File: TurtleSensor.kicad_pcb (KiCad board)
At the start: 2 copper layers, 30 x 30 mm, 14 parts, among them IC1 ATMEGA328P-A, J2 FTDIConnector, U1 SI7021, U2 M24512

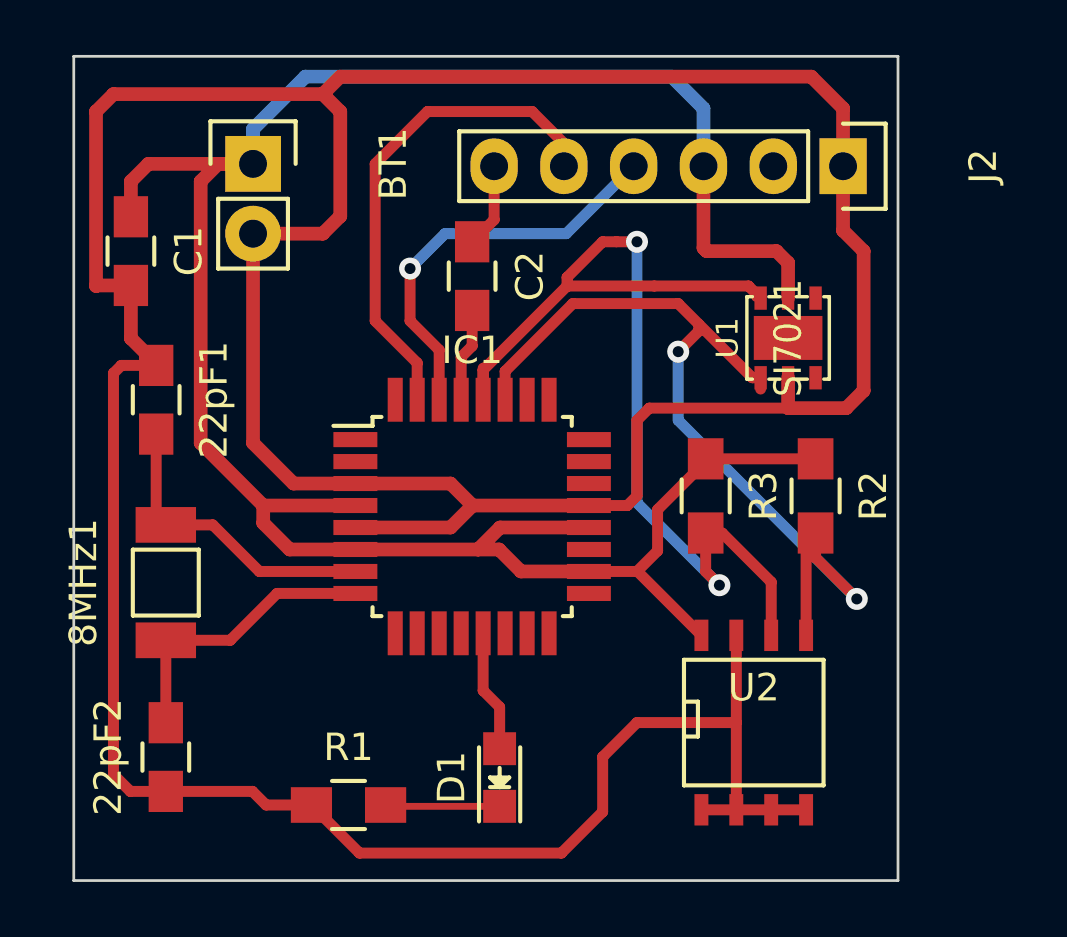
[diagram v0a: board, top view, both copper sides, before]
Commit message: sent board to be manufactured
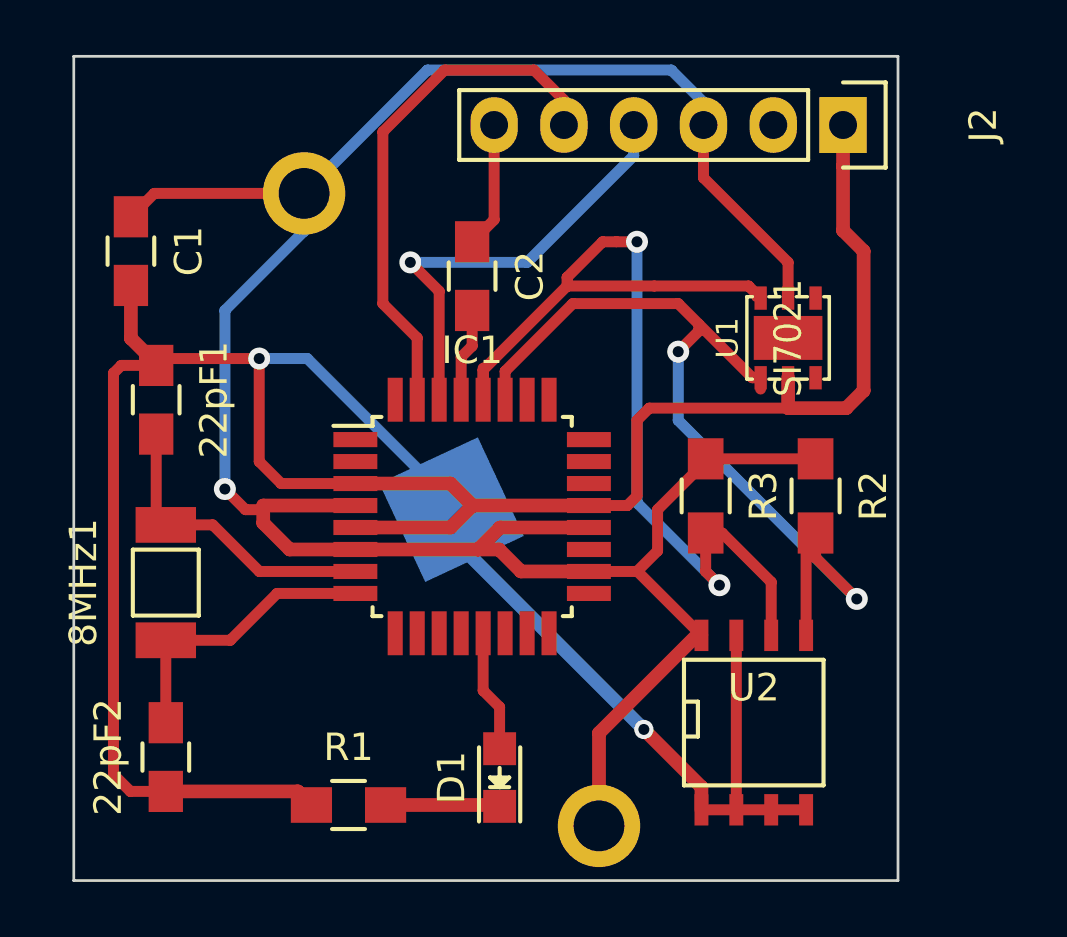
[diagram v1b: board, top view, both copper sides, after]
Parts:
- BT1: footprint Socket_Strips:Socket_Strip_Straight_1x02 -> footprints:2477Holder; moved to B.Cu
- moved BT1 14.5 mm to (143.8, 94.5), turned to 115 degrees
- moved J2 1.50 mm to (158.0, 80.5)
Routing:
- net GND: track 151.8 -> 115.4 mm, vias 0 -> 2
- net +BATT: track 84.6 -> 89.4 mm, vias 0 -> 1
- net Net-(C2-Pad1): track 3.38 -> 4.58 mm
- net /TX: track 20.0 -> 19.2 mm
- added copper zone on B.Cu, net GND
- added copper zone on F.Cu, net GND
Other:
- net class Default: trace_width 0.4 -> 0.5; via_dia 0.8 -> 0.7

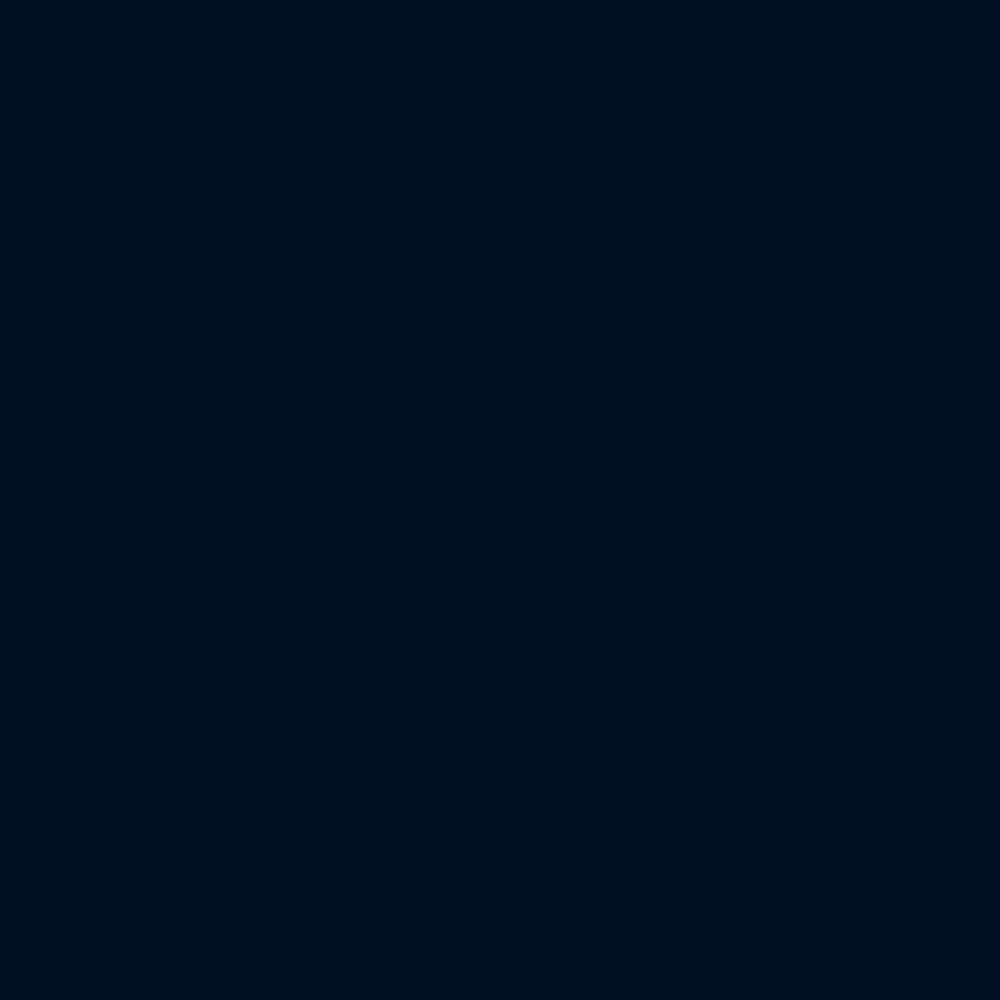
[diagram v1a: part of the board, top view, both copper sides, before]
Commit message: imported dxf
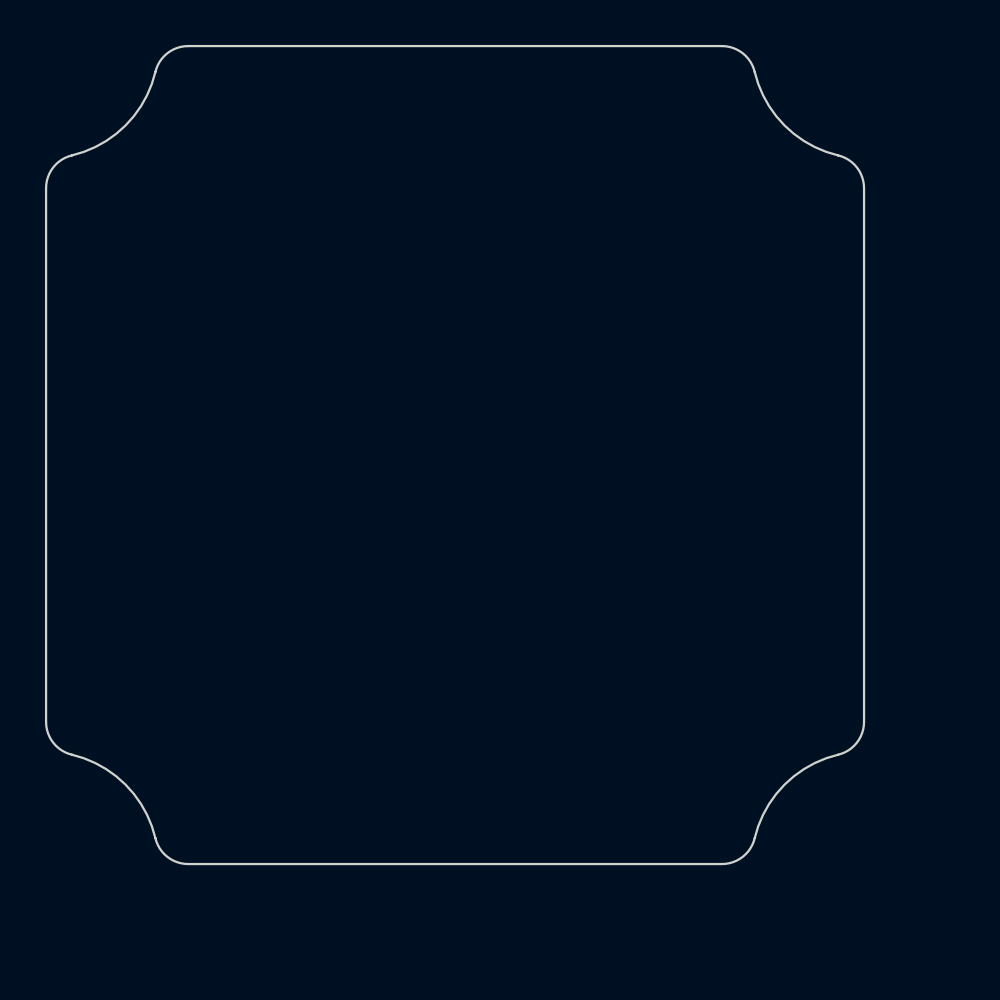
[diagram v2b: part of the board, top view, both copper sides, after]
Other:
- board size 30 x 30 mm -> 48.2 x 78.2 mm
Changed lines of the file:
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@@
     (area 128.855 74.915475 164.075 108.325)
     (thickness 1.6)
-    (drawings 4)
+    (drawings 20)
     (tracks 160)
     (zones 0)
@@
       (net 4 +BATT))
   )
+  (gr_arc (start 146.7 59.875445) (end 147.046154 61.334957) (angle -76.6576362) (layer Edge.Cuts) (width 0.1))
+  (gr_line (start 148.2 36.124555) (end 148.2 59.875445) (layer Edge.Cuts) (width 0.1))
+  (gr_arc (start 146.7 36.124555) (end 148.2 36.124555) (angle -76.6576362) (layer Edge.Cuts) (width 0.1))
+  (gr_arc (start 148.2 29.8) (end 143.334957 30.953846) (angle -63.31527241) (layer Edge.Cuts) (width 0.1))
+  (gr_arc (start 141.875445 31.3) (end 143.334957 30.953846) (angle -76.6576362) (layer Edge.Cuts) (width 0.1))
+  (gr_line (start 118.124555 29.8) (end 141.875445 29.8) (layer Edge.Cuts) (width 0.1))
+  (gr_arc (start 118.124555 31.3) (end 118.124555 29.8) (angle -76.6576362) (layer Edge.Cuts) (width 0.1))
+  (gr_arc (start 111.8 29.8) (end 112.953846 34.665043) (angle -63.31527241) (layer Edge.Cuts) (width 0.1))
+  (gr_arc (start 113.3 36.124555) (end 112.953846 34.665043) (angle -76.6576362) (layer Edge.Cuts) (width 0.1))
+  (gr_line (start 111.8 59.875445) (end 111.8 36.124555) (layer Edge.Cuts) (width 0.1))
+  (gr_arc (start 113.3 59.875445) (end 111.8 59.875445) (angle -76.6576362) (layer Edge.Cuts) (width 0.1))
+  (gr_arc (start 111.8 66.2) (end 116.665043 65.046154) (angle -63.31527241) (layer Edge.Cuts) (width 0.1))
+  (gr_arc (start 118.124555 64.7) (end 116.665043 65.046154) (angle -76.6576362) (layer Edge.Cuts) (width 0.1))
+  (gr_line (start 141.875445 66.2) (end 118.124555 66.2) (layer Edge.Cuts) (width 0.1))
+  (gr_arc (start 141.875445 64.7) (end 141.875445 66.2) (angle -76.6576362) (layer Edge.Cuts) (width 0.1))
+  (gr_arc (start 148.2 66.2) (end 147.046154 61.334957) (angle -63.31527241) (layer Edge.Cuts) (width 0.1))
   (gr_line (start 130 108) (end 130 78) (angle 90) (layer Edge.Cuts) (width 0.1))
   (gr_line (start 160 108) (end 130 108) (angle 90) (layer Edge.Cuts) (width 0.1))
@@
   (segment (start 137.4 97.55) (end 140.25 97.55) (width 0.4) (layer F.Cu) (net 2))
   (segment (start 135.695 99.255) (end 137.4 97.55) (width 0.4) (layer F.Cu) (net 2))
-  (segment (start 143.75 94.5) (end 143.75 95.5) (width 0.5) (layer B.Cu) (net 3) (status C00000))
-  (segment (start 143.75 95.5) (end 150.75 102.5) (width 0.5) (layer B.Cu) (net 3) (status 400000))
-  (segment (start 152.845 104.595) (end 152.845 105.425) (width 0.5) (layer F.Cu) (net 3) (status 800000))
+  (segment (start 143.75 94.5) (end 143.75 95.5) (width 0.5) (layer B.Cu) (net 3))
+  (segment (start 143.75 95.5) (end 150.75 102.5) (width 0.5) (layer B.Cu) (net 3))
+  (segment (start 152.845 104.595) (end 152.845 105.425) (width 0.5) (layer F.Cu) (net 3))
   (segment (start 150.75 102.5) (end 152.845 104.595) (width 0.5) (layer F.Cu) (net 3))
   (via (at 150.75 102.5) (size 0.7) (drill 0.4) (layers F.Cu B.Cu) (net 3))
-  (segment (start 133.35 104.755) (end 138.155 104.755) (width 0.5) (layer F.Cu) (net 3) (status C00000))
-  (segment (start 138.155 104.755) (end 138.65 105.25) (width 0.5) (layer F.Cu) (net 3) (status C00000))
+  (segment (start 133.35 104.755) (end 138.155 104.755) (width 0.5) (layer F.Cu) (net 3))
+  (segment (start 138.155 104.755) (end 138.65 105.25) (width 0.5) (layer F.Cu) (net 3))
   (segment (start 136.75 89) (end 133.25 89) (width 0.4) (layer F.Cu) (net 3))
   (segment (start 133.25 89) (end 133 89.25) (width 0.4) (layer F.Cu) (net 3))
@@
   (segment (start 143.715 93.55) (end 144.515 94.35) (width 0.5) (layer F.Cu) (net 3))
   (segment (start 156 90.805) (end 156 89.7) (width 0.5) (layer F.Cu) (net 3))
-  (segment (start 149.117252 106.010109) (end 149.117252 102.632748) (width 0.5) (layer F.Cu) (net 4) (status 400000))
-  (segment (start 149.117252 102.632748) (end 152.76 98.99) (width 0.5) (layer F.Cu) (net 4) (status 800000))
-  (segment (start 152.76 98.99) (end 152.845 99.075) (width 0.5) (layer F.Cu) (net 4) (status C00000))
+  (segment (start 149.117252 106.010109) (end 149.117252 102.632748) (width 0.5) (layer F.Cu) (net 4))
+  (segment (start 149.117252 102.632748) (end 152.76 98.99) (width 0.5) (layer F.Cu) (net 4))
+  (segment (start 152.76 98.99) (end 152.845 99.075) (width 0.5) (layer F.Cu) (net 4))
   (segment (start 152.92 80.5) (end 152.92 79.67) (width 0.4) (layer B.Cu) (net 4))
   (segment (start 152.92 79.67) (end 151.75 78.5) (width 0.4) (layer B.Cu) (net 4))
@@
   (segment (start 145.5 101.685) (end 145.5 103.20098) (width 0.4) (layer F.Cu) (net 7))
   (segment (start 144.9 101.085) (end 145.5 101.685) (width 0.4) (layer F.Cu) (net 7))
-  (segment (start 141.35 105.25) (end 145.45098 105.25) (width 0.5) (layer F.Cu) (net 8) (status C00000))
-  (segment (start 145.45098 105.25) (end 145.5 105.29902) (width 0.5) (layer F.Cu) (net 8) (status C00000))
+  (segment (start 141.35 105.25) (end 145.45098 105.25) (width 0.5) (layer F.Cu) (net 8))
+  (segment (start 145.45098 105.25) (end 145.5 105.29902) (width 0.5) (layer F.Cu) (net 8))
   (segment (start 141.39902 105.29902) (end 141.35 105.25) (width 0.25) (layer F.Cu) (net 8))
   (segment (start 157 95.35) (end 157 96.25) (width 0.4) (layer F.Cu) (net 9))

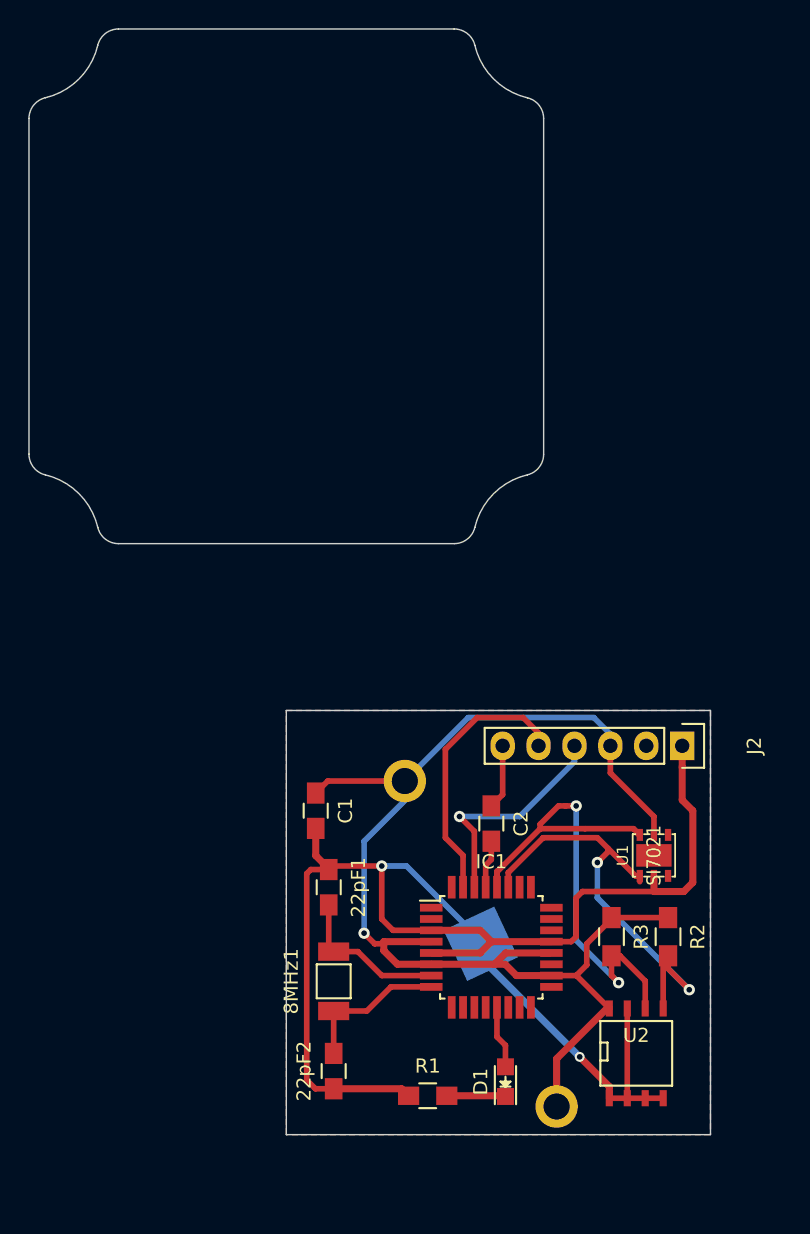
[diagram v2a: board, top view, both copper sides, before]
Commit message: fixed programming resistor, pcb is now circular v4
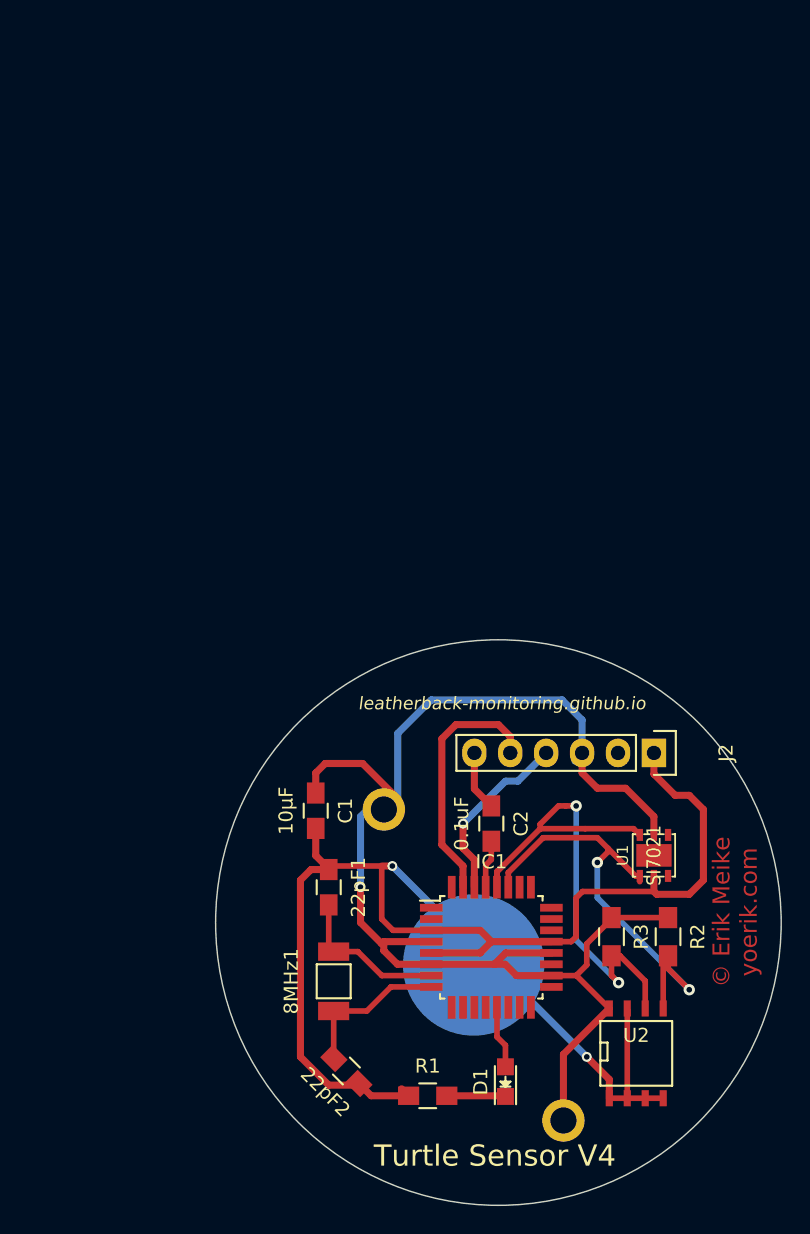
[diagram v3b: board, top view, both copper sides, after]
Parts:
- moved J2 2.06 mm to (156.0, 81.0)
- moved BT1 1.58 mm to (143.2, 96.0), turned to 120 degrees
- moved 22pF2 0.90 mm to (134.2, 103.5), turned to 135 degrees
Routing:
- net +BATT: track 89.4 -> 96.5 mm
- net /RX: track 16.3 -> 12.8 mm
- net GND: track 115.4 -> 113.5 mm
- net /TX: track 19.2 -> 17.9 mm
- removed copper zone on B.Cu, net GND
- removed copper zone on F.Cu, net GND
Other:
- board size 48.2 x 78.2 mm -> 40 x 40 mm
- rule trace_min: 0.3 -> 0.2
- board text added: "Turtle Sensor V4"
- board text added: "leatherback-monitoring.github.io"
- board text added: "© Erik Meike yoerik.com"

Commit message: before copper fill
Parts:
- removed 8MHz1: Crystal, footprints:2-SMD
- added 32KHz1: Crystal, Resistors_SMD:R_0805_HandSoldering, F.Cu at (135.0, 97.0)
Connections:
- D1 pad 2: Net-(D1-Pad2) -> /SCK
- IC1 pad 13: Net-(D1-Pad2) -> (no net)
- IC1 pad 17: (no net) -> /SCK
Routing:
- net /SCK: track 0.00 -> 7.76 mm
- net Net-(D1-Pad2): track 4.45 -> 0.00 mm
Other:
- net class Default: trace_width 0.5 -> 0.4
- net class Power: trace_width 0.5 -> 0.7
